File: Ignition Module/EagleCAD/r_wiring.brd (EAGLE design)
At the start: 83.5 x 50.8 mm, 51 parts, among them T1 BC848, T2 BC848, T3 BC848, T4 ZXTP2041F, T5 BUB323Z

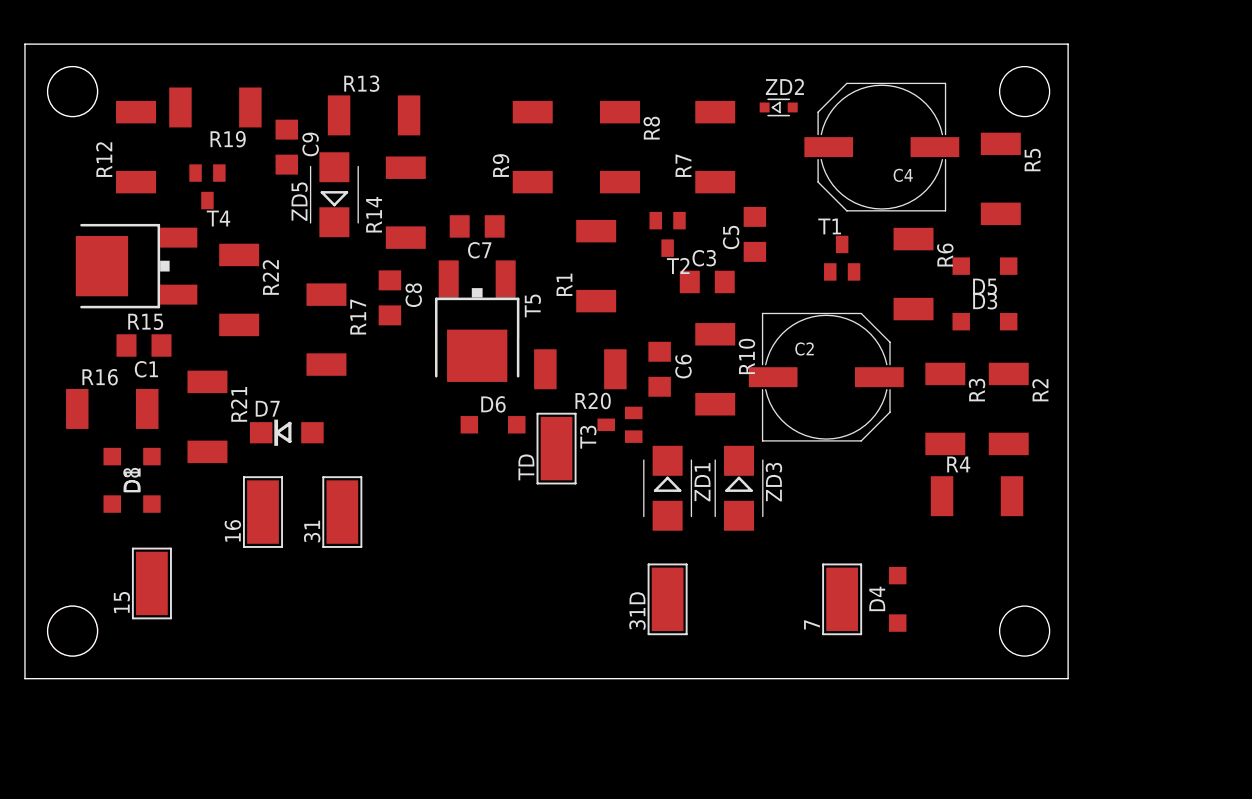
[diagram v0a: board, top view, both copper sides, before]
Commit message: Updated board layout and routing
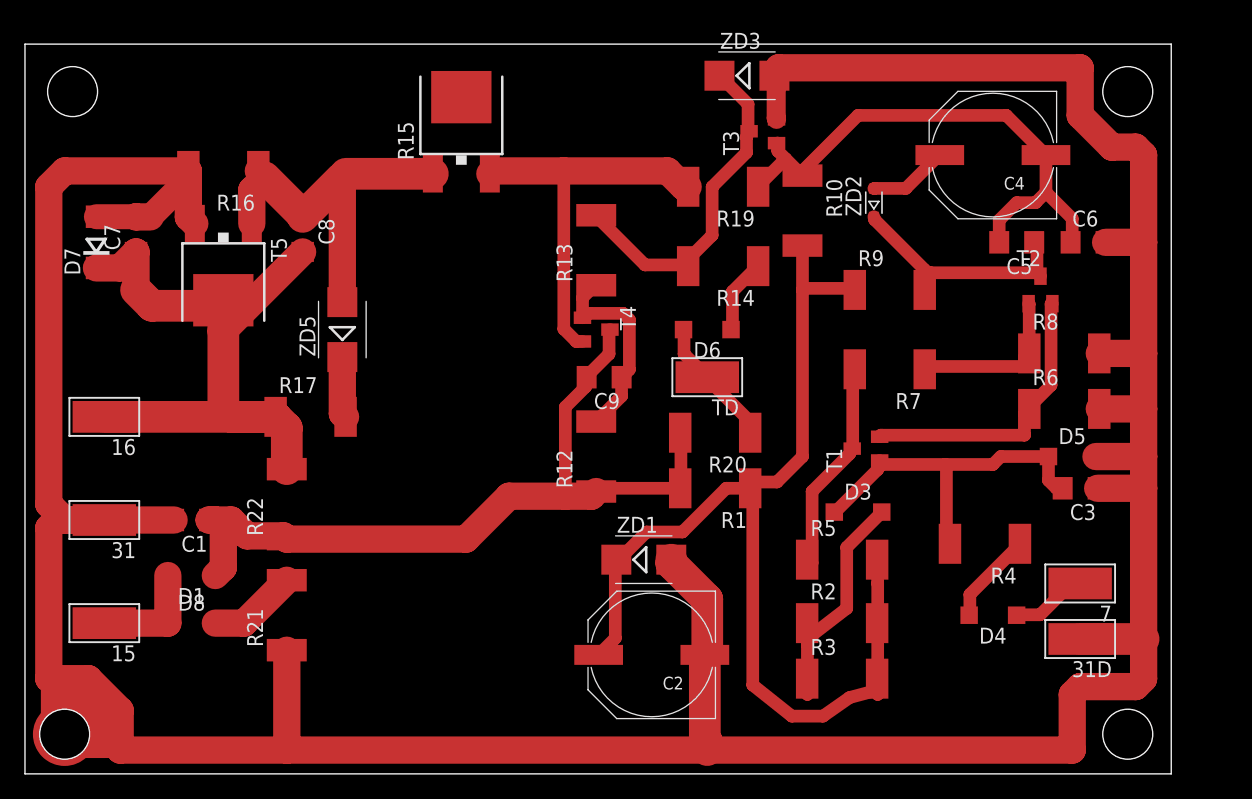
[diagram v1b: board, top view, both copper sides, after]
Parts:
- moved R12 44.4 mm to (45.7, 34.3)
- moved R19 41.1 mm to (55.9, 55.9)
- moved R8 39.2 mm to (83.2, 42.5), turned to 0 degrees
- moved C6 35.8 mm to (85.1, 51.4), turned to 0 degrees
- moved C3 34.1 mm to (84.5, 31.8), turned to 180 degrees
- moved 31D 33.2 mm to (84.5, 19.7), turned to 90 degrees
- moved T4 33.1 mm to (45.7, 44.5), turned to 270 degrees
- moved ZD3 33.0 mm to (57.8, 64.8), turned to 0 degrees
- moved R5 33.0 mm to (65.4, 26.0), turned to 0 degrees
- moved C9 31.4 mm to (46.4, 40.6), turned to 180 degrees
- moved R9 30.8 mm to (69.2, 47.6), turned to 0 degrees
- moved T2 30.2 mm to (81.3, 47.6), turned to 0 degrees
- moved R15 29.0 mm to (34.9, 61.0), turned to 0 degrees
- moved C7 27.3 mm to (8.89, 52.1), turned to 90 degrees
- moved C2 26.3 mm to (50.2, 18.4), turned to 180 degrees
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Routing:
- net GND: track 0.00 -> 302.2 mm
- net N$31: track 0.00 -> 91.4 mm
- net N$21: track 0.00 -> 64.7 mm
- net N$29: track 0.00 -> 54.8 mm
- net N$16: track 0.00 -> 44.0 mm
- net N$1: track 0.00 -> 31.1 mm
- net N$2: track 0.00 -> 31.1 mm
- net N$4: track 0.00 -> 29.6 mm
- net N$15: track 0.00 -> 27.3 mm
- net N$14: track 0.00 -> 23.1 mm
- net N$18: track 0.00 -> 20.4 mm
- net N$11: track 0.00 -> 20.4 mm
- net N$7: track 0.00 -> 17.8 mm
- net N$22: track 0.00 -> 16.4 mm
- net N$6: track 0.00 -> 13.3 mm
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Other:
- board size 83.5 x 50.8 mm -> 91.7 x 58.4 mm

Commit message: Circuit and board updates
Updated circuit with functional layout and annotations. Revised and
added component ratings. Added BOM. Updated board layout. Updates
provided by djenka018 of http://forum.w116.org
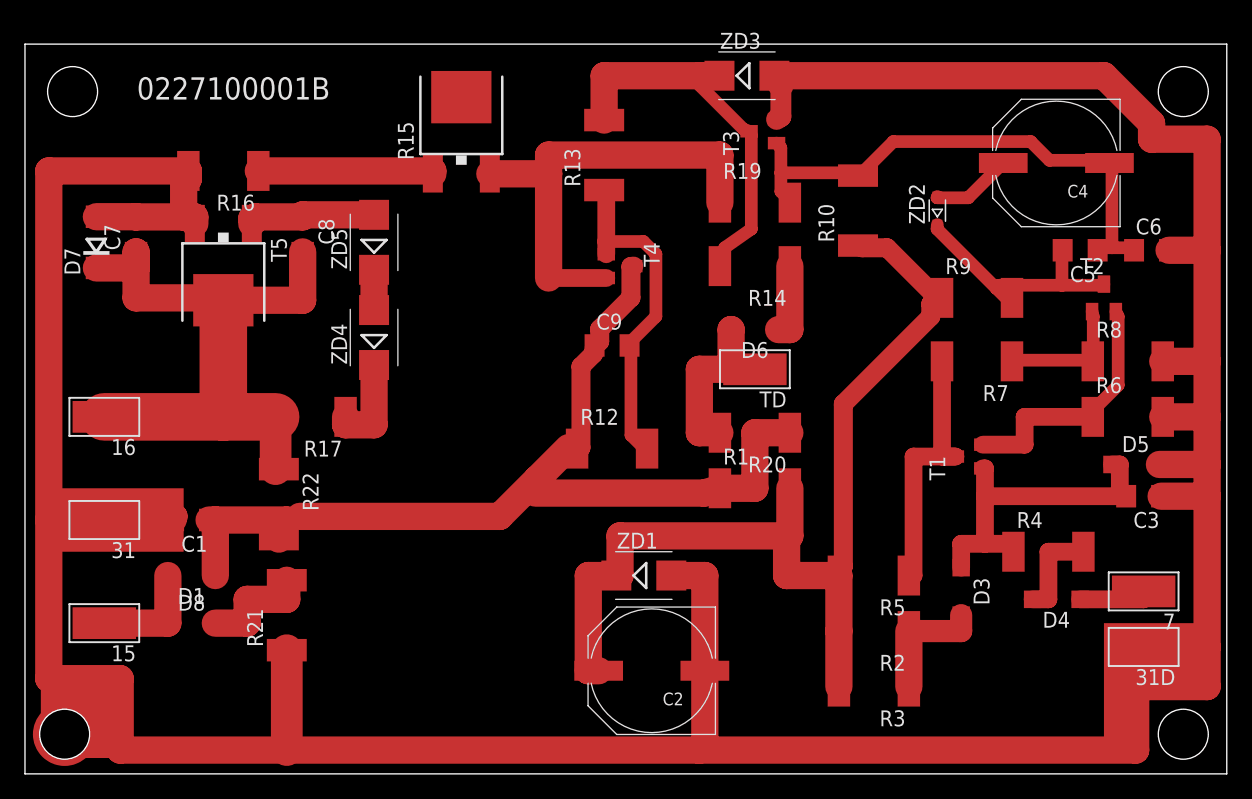
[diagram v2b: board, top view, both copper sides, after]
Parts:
- added ZD4: BZG05C51, diode:SMB
- 15, 16, 31, 31D, 7, TD: value WIREPADSMD5-2,5 -> (none)
- C1: value 1u -> 1u/100V
- C2: value 22u -> 22u/35V
- C3: value 6.8n -> 6.8n/400V
- C4: value 8.2u -> 8.2u/20V
- C5: value 0.47u -> 0.47u/100V
- C6, C9: value 10n -> 10n/160V
- C7: value 10nF -> 10n/400V
- C8: value 680p -> 680p/400V
- D1, D8: value 1N4148 -> BYG20D
- R15: value 33 -> 33/20W
- R21: value 22 -> 22/2W
- ZD5: value BZG05C100 -> BZG05C39
- moved D3 10.4 mm to (74.9, 23.5), turned to 270 degrees
- moved T1 8.28 mm to (75.6, 34.3)
- moved R13 7.65 mm to (46.4, 58.4)
- moved ZD5 7.43 mm to (27.9, 51.4)
- moved R7 7.01 mm to (76.2, 41.9)
- moved R9 7.01 mm to (76.2, 47.0)
- moved T4 5.43 mm to (47.6, 49.5)
- moved D4 5.24 mm to (82.5, 22.9)
- moved D5 5.12 mm to (88.9, 33.7)
- moved R4 5.12 mm to (81.9, 26.7), turned to 0 degrees
- moved ZD2 5.12 mm to (73.0, 54.0)
- moved C4 5.12 mm to (82.5, 57.8)
- moved C5 5.12 mm to (84.5, 50.8)
- moved C6 5.12 mm to (90.2, 50.8)
- moved R8 5.12 mm to (88.3, 41.9)
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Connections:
- removed net N$1: C8.1, R15.1, R16.1, T5.1, ZD5.A
- removed net N$2 (its old number): R15.3, R19.2, T4.C
- removed net N$20 (its old number): D6.A, R20.1, TD.1
- removed net N$28: R17.2, ZD5.C
- removed net N$29: 16.1, C7.1, C8.2, D7.C, R17.1, R22.2, T5.4
- removed net N$31: C2.+, R1.1, R10.2, R2.2, R3.2, R5.2, R9.1, ZD1.C
- new net N$11: C5.2, R9.2, T2.3, ZD2.C
- new net N$13: R15.3, R19.1, T4.C
- new net N$14: C1.1, C9.1, D1.C, R1.1, R12.1, R20.1, R22.2, T4.E
- new net N$15: D6.A, R20.2, TD.1
- new net N$23: ZD4.A, ZD5.C
- new net N$25: C8.1, T5.1, ZD5.A
- new net N$3: D4.A, R4.2
- new net N$8: C2.+, R1.2, R10.1, R2.2, R3.2, R5.2, R9.1, ZD1.C
- net N$12: now also C4.-, C5.1, C6.1, R10.2, R19.2, T3.1; no longer D4.A, R4.1
- net N$16: now also C9.2, R12.2, R13.1, T4.B; no longer C4.-, C5.2, C6.1, R10.1, R19.1, T3.1
- net N$18: now also R15.1, R16.1; no longer C5.1, R9.2, T2.3, ZD2.C
- net N$21: now also R17.1, ZD4.C; no longer C1.1, C9.2, D1.C, R1.2, R12.1, R20.2, R22.1, T4.E
- net N$22: now also 16.1, C7.1, C8.2, D7.C, R17.2, R22.1, T5.4; no longer C9.1, R12.2, R13.1, T4.B
- net N$4: now also R4.1; no longer R4.2
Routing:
- net N$31: track 91.4 -> 0.00 mm
- net N$8: track 0.00 -> 81.7 mm
- net N$14: track 0.00 -> 80.6 mm
- net N$21: track 64.7 -> 7.70 mm
- net N$29: track 54.8 -> 0.00 mm
- net N$13: track 0.00 -> 36.7 mm
- net N$22: track 16.4 -> 53.0 mm
- net N$12: track 7.40 -> 43.3 mm
- net N$1: track 31.1 -> 0.00 mm
- net N$2 (its old number): track 31.1 -> 0.00 mm
- net N$11: track 0.00 -> 20.9 mm
- net N$16: track 44.0 -> 26.8 mm
- net N$15: track 0.00 -> 14.4 mm
- net N$25: track 0.00 -> 10.5 mm
- net N$10: track 20.4 -> 9.91 mm
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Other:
- board size 91.7 x 58.4 mm -> 96.2 x 58.4 mm
- board text added: "0227100001B"

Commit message: Fix missing net
+ Fix missing net T5.B -> R15:R16
+ Rename C8 <-> C9
+ Replace D8 with 1N4148
+ Replace parallel R2 (24k) + R3 (41.2k) with 15.4k R2 only
+ Update PCB layout + routing
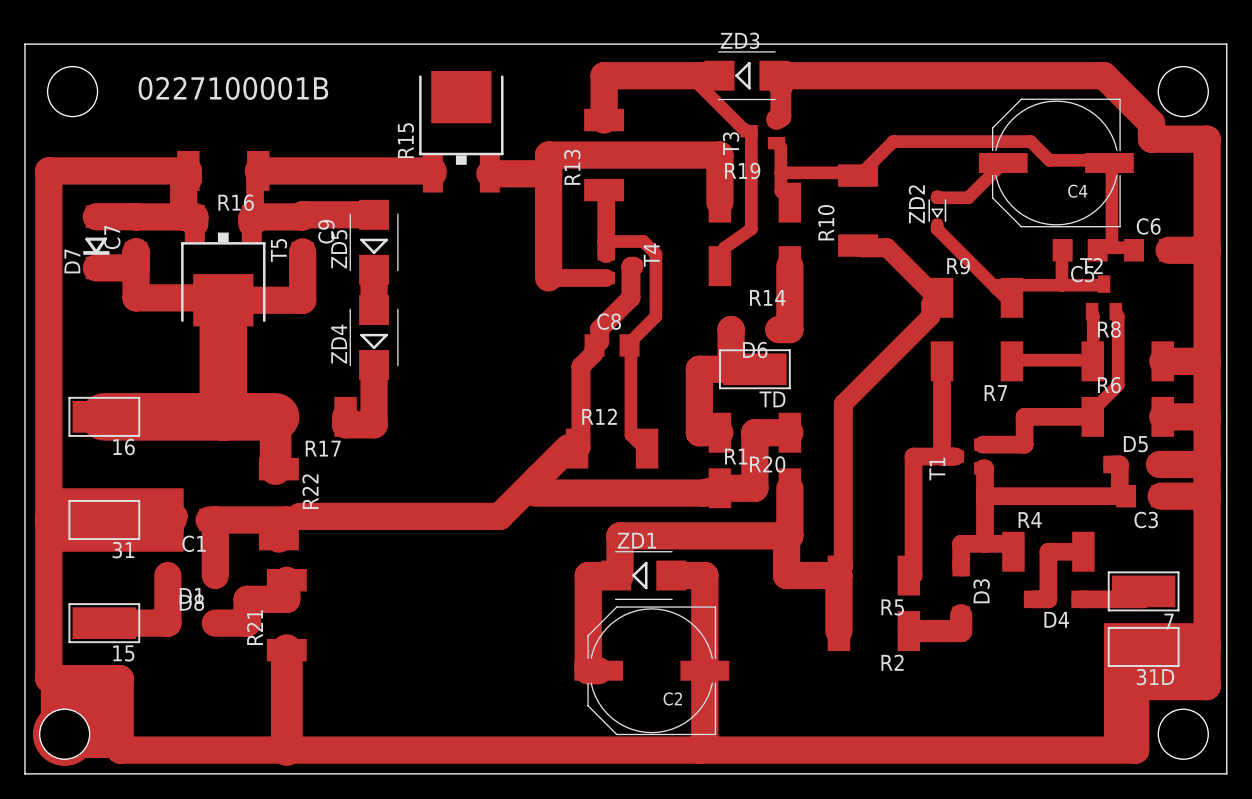
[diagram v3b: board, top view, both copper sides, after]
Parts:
- removed R3: 41.2k, resistor:R2512
- C8: value 680p/400V -> 10n/160V
- C9: value 10n/160V -> 680p/400V
- D1, D8: value BYG20D -> 1N4148
- R2: value 24k -> 15.4k
- moved C8 26.3 mm to (47.0, 43.2), turned to 0 degrees
- moved C9 26.3 mm to (22.2, 52.1), turned to 270 degrees
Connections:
- removed net N$18: R15.1, R16.1
- net N$10: no longer R3.1
- net N$14: now also C8.1; no longer C9.1
- net N$16: now also C8.2; no longer C9.2
- net N$22: now also C9.2; no longer C8.2
- net N$25: now also C9.1, R15.1, R16.1; no longer C8.1
- net N$8: no longer R3.2
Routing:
- net N$25: track 10.5 -> 28.5 mm
- net N$18: track 14.2 -> 0.00 mm
- net N$10: track 9.91 -> 5.46 mm
- net N$8: track 81.7 -> 77.2 mm
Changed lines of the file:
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@@
 <?xml version="1.0" encoding="utf-8"?>
 <!DOCTYPE eagle SYSTEM "eagle.dtd">
-<eagle version="7.4.0">
+<eagle version="7.5.0">
 <drawing>
 <settings>
@@
 <element name="C5" library="rcl" package="C1206" value="0.47u/100V" x="84.455" y="50.8" rot="R180"/>
 <element name="C6" library="rcl" package="C1206" value="10n/160V" x="90.17" y="50.8"/>
-<element name="C8" library="rcl" package="C1206" value="680p/400V" x="22.225" y="52.07" rot="R270"/>
-<element name="C9" library="rcl" package="C1206" value="10n/160V" x="46.99" y="43.18"/>
-<element name="D1" library="diode" package="SOD123" value="BYG20D" x="13.335" y="24.765" rot="R180"/>
+<element name="C9" library="rcl" package="C1206" value="680p/400V" x="22.225" y="52.07" rot="R270"/>
+<element name="C8" library="rcl" package="C1206" value="10n/160V" x="46.99" y="43.18"/>
+<element name="D1" library="diode" package="SOD123" value="1N4148" x="13.335" y="24.765" rot="R180"/>
 <element name="D3" library="diode" package="SOD123" value="1N4148" x="74.93" y="23.495" rot="R270"/>
 <element name="D4" library="diode" package="SOD123" value="1N4148" x="82.55" y="22.86" rot="R180"/>
@@
 <element name="D6" library="diode" package="SOD123" value="1N4148" x="58.42" y="44.45" rot="R180"/>
 <element name="D7" library="diode" package="DO214AC" value="BYG20D" x="5.715" y="51.435" rot="R90"/>
-<element name="D8" library="diode" package="SOD123" value="BYG20D" x="13.335" y="20.955"/>
+<element name="D8" library="diode" package="SOD123" value="1N4148" x="13.335" y="20.955"/>
 <element name="R1" library="resistor" package="R2512" value="220" x="58.42" y="31.75"/>
 <element name="R10" library="resistor" package="R2512" value="3.46k" x="66.675" y="53.975" rot="R90"/>
@@
 <element name="R17" library="resistor" package="R2512" value="330" x="22.86" y="37.465" rot="R180"/>
 <element name="R19" library="rcl" package="R2512" value="15k" x="58.42" y="54.61"/>
-<element name="R2" library="resistor" package="R2512" value="24k" x="67.945" y="20.32" rot="R180"/>
+<element name="R2" library="resistor" package="R2512" value="15.4k" x="67.945" y="20.32" rot="R180"/>
 <element name="R20" library="resistor" package="R2512" value="2.2k" x="58.42" y="36.195" rot="R180"/>
 <element name="R21" library="resistor" package="R2512" value="22/2W" x="20.955" y="21.59" rot="R90"/>
 <element name="R22" library="rcl" package="R2512" value="10k" x="20.32" y="30.48" rot="R270"/>
-<element name="R3" library="resistor" package="R2512" value="41.2k" x="67.945" y="15.875" rot="R180"/>
 <element name="R4" library="resistor" package="R2512" value="3.3k" x="81.915" y="26.67"/>
 <element name="R5" library="resistor" package="R2512" value="560" x="67.945" y="24.765" rot="R180"/>
@@
 <contactref element="ZD1" pad="C"/>
 <contactref element="C2" pad="+"/>
-<contactref element="R3" pad="2"/>
 <contactref element="R2" pad="2"/>
 <contactref element="R5" pad="2"/>
@@
 <wire x1="60.96" y1="24.765" x2="60.96" y2="27.94" width="2.1844" layer="1"/>
 <wire x1="65.145" y1="24.765" x2="65.145" y2="20.32" width="2.1844" layer="1"/>
-<wire x1="65.145" y1="20.32" x2="65.145" y2="15.875" width="2.1844" layer="1"/>
 <wire x1="69" y1="51" x2="67" y2="51" width="1.524" layer="1"/>
 <wire x1="73" y1="47" x2="69" y2="51" width="1.524" layer="1"/>
@@
 </signal>
 <signal name="N$10">
-<contactref element="R3" pad="1"/>
 <contactref element="R2" pad="1"/>
 <contactref element="D3" pad="A"/>
-<wire x1="70.745" y1="15.875" x2="70.745" y2="20.32" width="2.1844" layer="1"/>
 <wire x1="70.745" y1="20.32" x2="74.93" y2="20.32" width="1.778" layer="1"/>
 <wire x1="74.93" y1="20.32" x2="74.93" y2="21.595" width="1.778" layer="1"/>
@@
 <contactref element="R12" pad="2"/>
 <contactref element="T4" pad="B"/>
-<contactref element="C9" pad="2"/>
+<contactref element="C8" pad="2"/>
 <contactref element="R13" pad="1"/>
 <wire x1="46.355" y1="55.62" x2="46.525" y2="55.62" width="1.4224" layer="1"/>
@@
 <contactref element="R12" pad="1"/>
 <contactref element="R20" pad="1"/>
-<contactref element="C9" pad="1"/>
+<contactref element="C8" pad="1"/>
 <contactref element="D1" pad="C"/>
 <contactref element="C1" pad="1"/>
@@
 <wire x1="41.91" y1="48.58" x2="41.91" y2="56.92" width="2.1844" layer="1"/>
 </signal>
-<signal name="N$18">
-<contactref element="R15" pad="1"/>
-<contactref element="R16" pad="1"/>
-<wire x1="18.675" y1="57.15" x2="32.645" y2="57.15" width="2.1844" layer="1"/>
-<wire x1="32.645" y1="57.15" x2="32.645" y2="56.92" width="2.1844" layer="1"/>
-</signal>
 <signal name="N$19" class="1">
 <contactref element="D1" pad="A"/>
@@
 <contactref element="D7" pad="C"/>
 <contactref element="C7" pad="1"/>
-<contactref element="C8" pad="2"/>
+<contactref element="C9" pad="2"/>
 <contactref element="T5" pad="4"/>
 <wire x1="20.06" y1="37.465" x2="15.875" y2="37.465" width="3.81" layer="1"/>
@@
 <signal name="N$25">
 <contactref element="ZD5" pad="A"/>
-<contactref element="C8" pad="1"/>
+<contactref element="C9" pad="1"/>
 <contactref element="T5" pad="1"/>
 <wire x1="27.94" y1="53.635" x2="22.225" y2="53.635" width="2.1844" layer="1"/>
@@
 <wire x1="18.415" y1="53.34" x2="18.155" y2="53.34" width="2.1844" layer="1"/>
 <wire x1="18.155" y1="53.34" x2="18.155" y2="52.935" width="2.1844" layer="1"/>
+<contactref element="R15" pad="1"/>
+<contactref element="R16" pad="1"/>
+<wire x1="18.675" y1="57.15" x2="32.645" y2="57.15" width="2.1844" layer="1"/>
+<wire x1="32.645" y1="57.15" x2="32.645" y2="56.92" width="2.1844" layer="1"/>
+<wire x1="19.05" y1="56.515" x2="18.415" y2="56.515" width="1.4224" layer="1"/>
+<wire x1="18.415" y1="56.515" x2="18.415" y2="53.34" width="1.4224" layer="1"/>
+<wire x1="18.415" y1="56.515" x2="18.675" y2="57.15" width="0" layer="19" extent="1-1"/>
 </signal>
 <signal name="N$26">
